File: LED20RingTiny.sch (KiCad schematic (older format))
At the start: 24 parts, among them IC1 ATTINY45-P, SW1 SW_Push

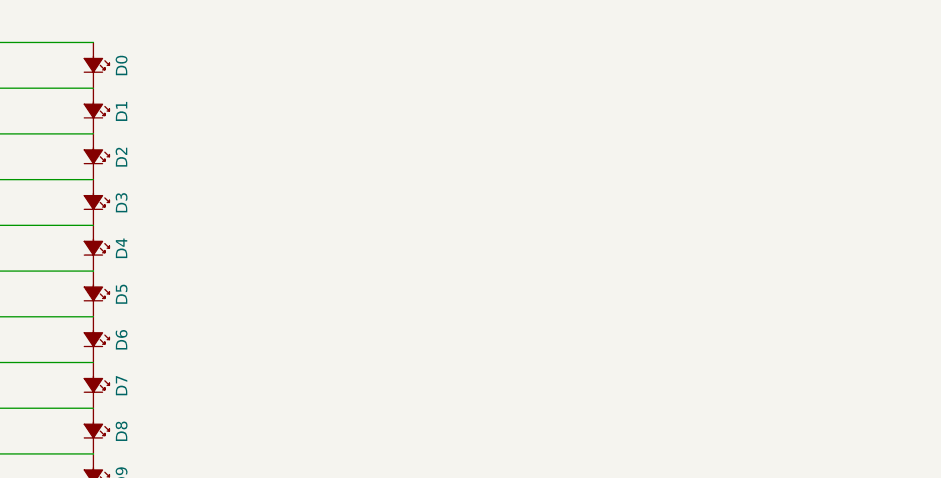
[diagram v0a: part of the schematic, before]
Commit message: Title text in schema
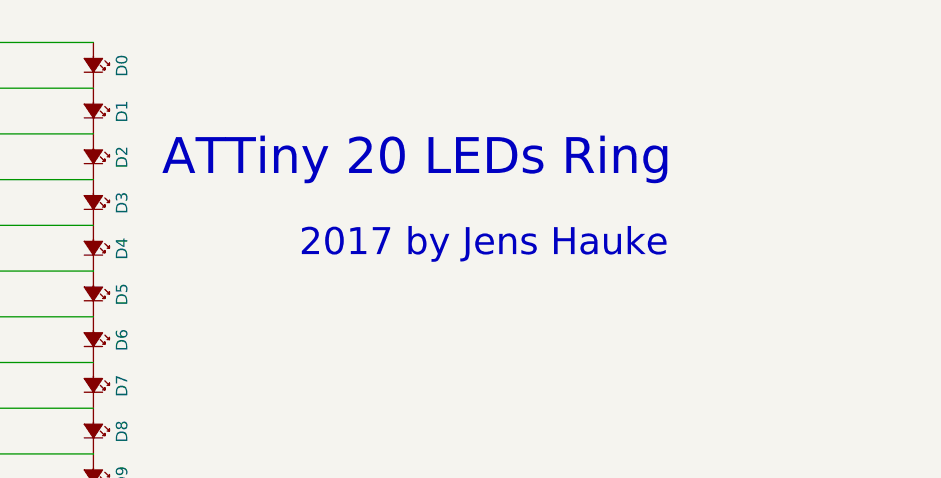
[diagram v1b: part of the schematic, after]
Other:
- note added: "2017 by Jens Hauke\n"
- note added: "ATTiny 20 LEDs Ring"
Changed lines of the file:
@@
 Wire Wire Line
 	9500 3700 9500 3800
+Text Notes 6850 1850 0    157  ~ 0
+ATTiny 20 LEDs Ring
+Text Notes 7450 2200 0    118  ~ 0
+2017 by Jens Hauke\n
 $EndSCHEMATC
